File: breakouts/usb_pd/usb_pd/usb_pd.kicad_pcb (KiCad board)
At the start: 4 copper layers, 33 x 18.2 mm, 32 parts, among them J101 USB_C_Receptacle_USB2.0, J102 Conn_01x04, J103 1725656, Q101 VBZA4435, U101 HUSB238

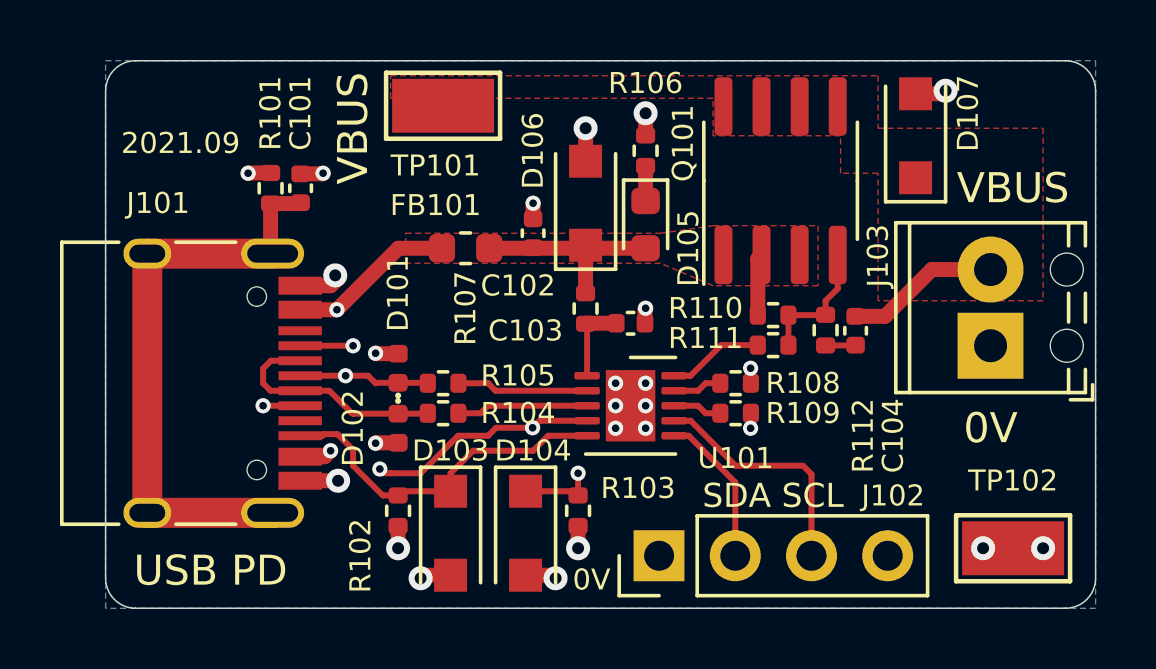
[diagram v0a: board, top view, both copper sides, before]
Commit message: added missing synth files
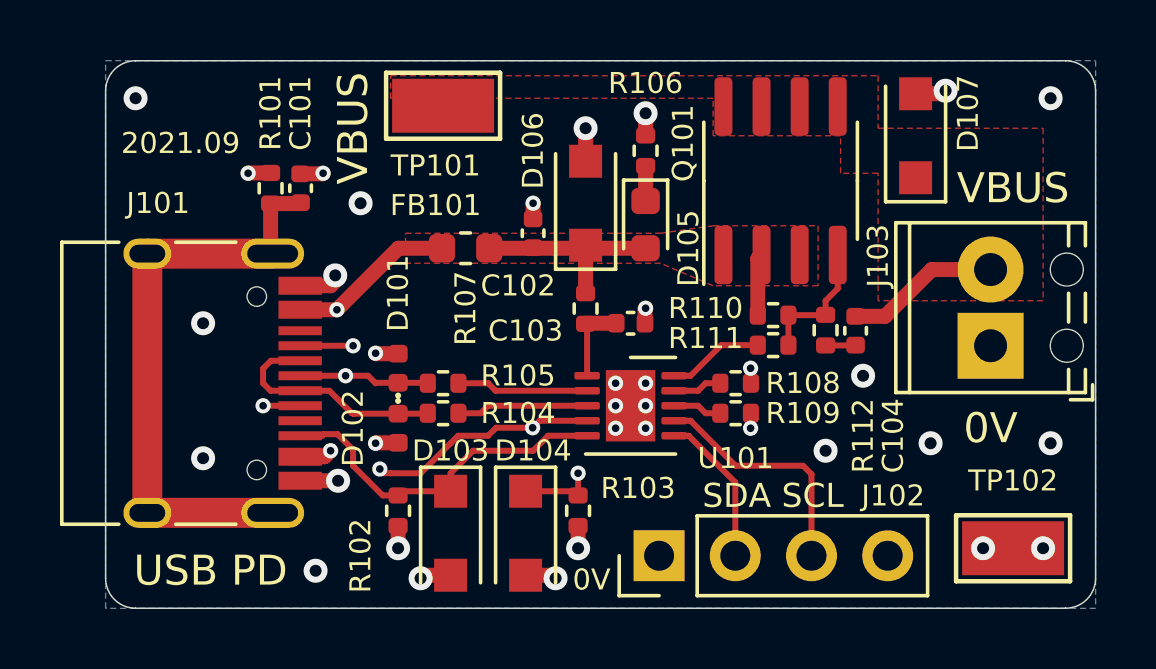
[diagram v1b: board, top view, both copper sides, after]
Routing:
- net GND: vias 25 -> 35
- added copper zone on In1.Cu, net GND
- added copper zone on In2.Cu, net GND
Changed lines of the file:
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@@
   (segment (start 87.23 112.02) (end 87.25 112) (width 0.5) (layer "F.Cu") (net 2))
   (via (at 89 118) (size 0.508) (drill 0.254) (layers "F.Cu" "B.Cu") (net 2))
+  (via (at 104 121.25) (size 0.8) (drill 0.4) (layers "F.Cu" "B.Cu") (net 2))
   (via (at 108 109.25) (size 0.8) (drill 0.4) (layers "F.Cu" "B.Cu") (net 2))
   (via (at 95.75 124.5) (size 0.8) (drill 0.4) (layers "F.Cu" "B.Cu") (net 2))
+  (via (at 111.5 109.5) (size 0.8) (drill 0.4) (layers "F.Cu" "B.Cu") (net 2))
   (via (at 94.25 113) (size 0.508) (drill 0.254) (layers "F.Cu" "B.Cu") (net 2))
   (via (at 98 119.75) (size 0.508) (drill 0.254) (layers "F.Cu" "B.Cu") (net 2))
   (via (at 98 119) (size 0.508) (drill 0.254) (layers "F.Cu" "B.Cu") (net 2))
+  (via (at 88.5 113) (size 0.8) (drill 0.4) (layers "F.Cu" "B.Cu") (net 2))
   (via (at 111.25 124.5) (size 0.8) (drill 0.4) (layers "F.Cu" "B.Cu") (net 2))
+  (via (at 105.25 118.75) (size 0.8) (drill 0.4) (layers "F.Cu" "B.Cu") (net 2))
   (via (at 98 120.5) (size 0.508) (drill 0.254) (layers "F.Cu" "B.Cu") (net 2))
   (via (at 97 119) (size 0.508) (drill 0.254) (layers "F.Cu" "B.Cu") (net 2))
   (via (at 97 119.75) (size 0.508) (drill 0.254) (layers "F.Cu" "B.Cu") (net 2))
+  (via (at 81 109.5) (size 0.8) (drill 0.4) (layers "F.Cu" "B.Cu") (net 2))
   (via (at 109.25 124.5) (size 0.8) (drill 0.4) (layers "F.Cu" "B.Cu") (net 2))
   (via (at 97 120.5) (size 0.508) (drill 0.254) (layers "F.Cu" "B.Cu") (net 2))
@@
   (via (at 98 110) (size 0.8) (drill 0.4) (layers "F.Cu" "B.Cu") (net 2))
   (via (at 96 110.5) (size 0.8) (drill 0.4) (layers "F.Cu" "B.Cu") (net 2))
+  (via (at 83.25 117) (size 0.8) (drill 0.4) (layers "F.Cu" "B.Cu") (net 2))
   (via (at 101.5 118.5) (size 0.508) (drill 0.254) (layers "F.Cu" "B.Cu") (net 2))
   (via (at 89.75 124.5) (size 0.8) (drill 0.4) (layers "F.Cu" "B.Cu") (net 2))
   (via (at 84.75 112) (size 0.508) (drill 0.254) (layers "F.Cu" "B.Cu") (net 2))
   (via (at 87.25 112) (size 0.508) (drill 0.254) (layers "F.Cu" "B.Cu") (net 2))
+  (via (at 111.5 121) (size 0.8) (drill 0.4) (layers "F.Cu" "B.Cu") (net 2))
   (via (at 95 125.5) (size 0.8) (drill 0.4) (layers "F.Cu" "B.Cu") (net 2))
+  (via (at 83.25 121.5) (size 0.8) (drill 0.4) (layers "F.Cu" "B.Cu") (net 2))
   (via (at 98 116.5) (size 0.508) (drill 0.254) (layers "F.Cu" "B.Cu") (net 2))
+  (via (at 87 125.25) (size 0.8) (drill 0.4) (layers "F.Cu" "B.Cu") (net 2))
   (via (at 90.5 125.5) (size 0.8) (drill 0.4) (layers "F.Cu" "B.Cu") (net 2))
+  (via (at 107.5 121) (size 0.8) (drill 0.4) (layers "F.Cu" "B.Cu") (net 2))
   (via (at 87.75 122.25) (size 0.8) (drill 0.4) (layers "F.Cu" "B.Cu") (net 2))
   (segment (start 101.74 116.73) (end 101.74 114.85) (width 0.5) (layer "F.Cu") (net 3))
@@
     )
   )
-  (zone locked (net 2) (net_name "GND") (layer "B.Cu") (hatch edge 0.508)
+  (zone locked (net 2) (net_name "GND") (layers "In1.Cu" "In2.Cu" "B.Cu") (hatch edge 0.508)
     (connect_pads yes (clearance 0.254))
     (min_thickness 0.254) (filled_areas_thickness no)
